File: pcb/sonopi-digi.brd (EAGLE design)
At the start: 65 x 20.3 mm, 11 parts, among them IC1 WM8804, J1 PLT133_T10W, J2 RASPI_BOARD_B+#_SMALL, X1 27MHz/15pF

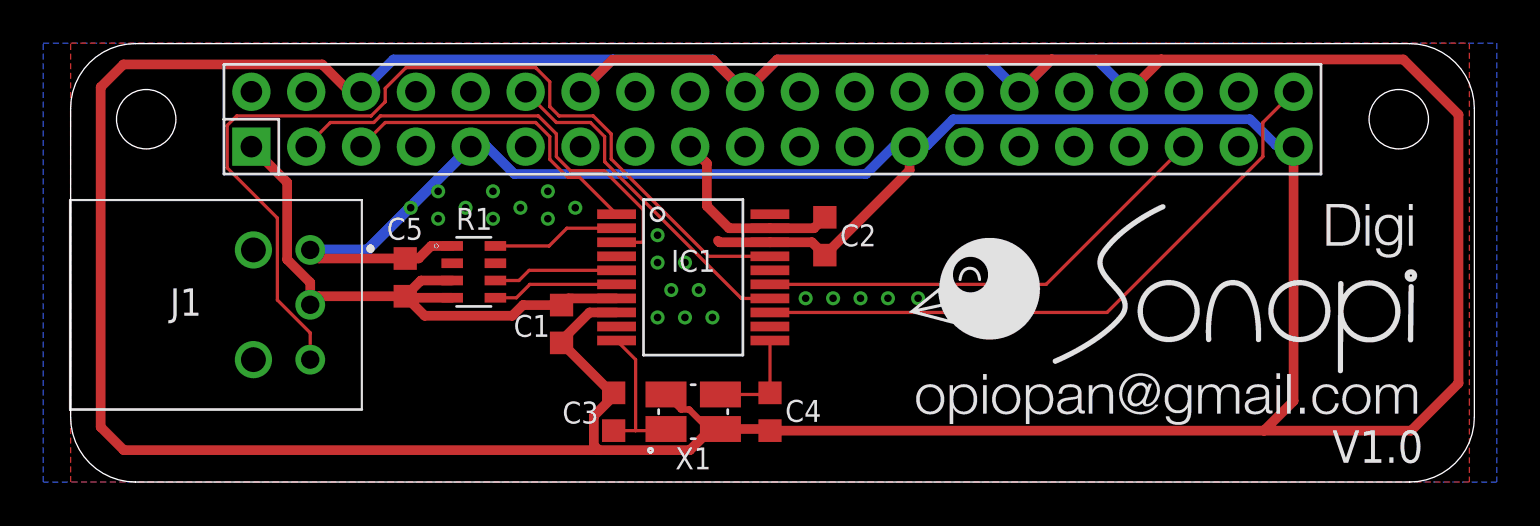
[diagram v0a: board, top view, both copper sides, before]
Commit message: fix a S/PDIF transmitter pin assign issue
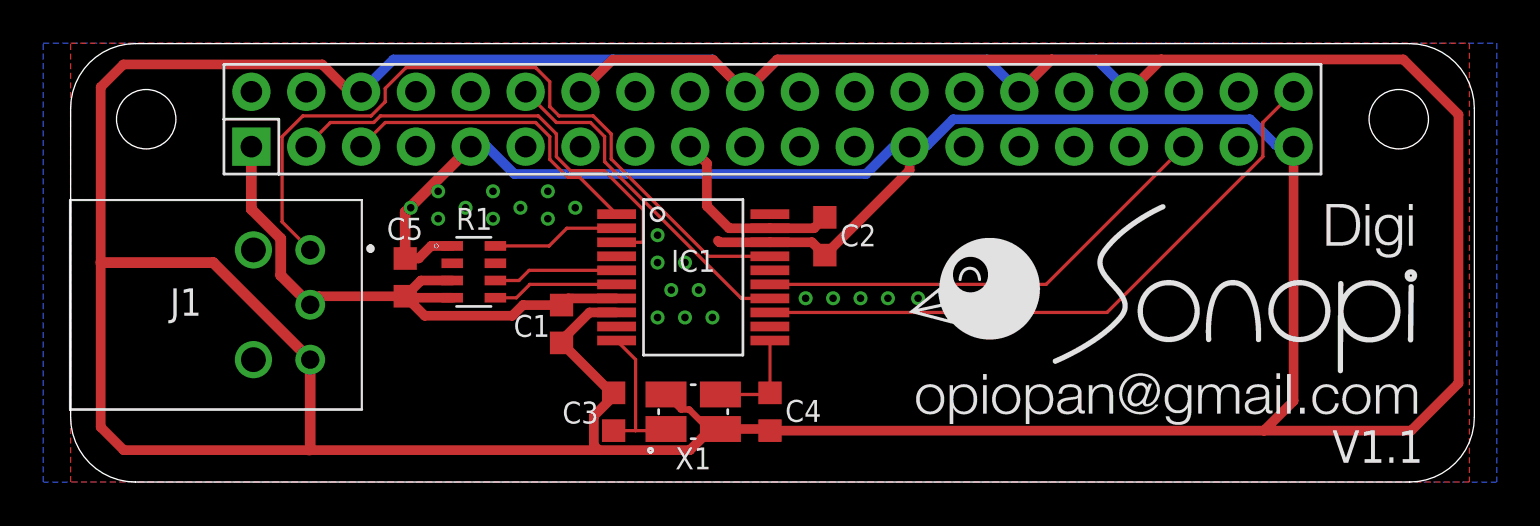
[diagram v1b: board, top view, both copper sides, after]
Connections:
- net GND: now also J1.3; no longer J1.1
- net TX0: now also J1.1; no longer J1.3
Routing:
- net TX0: track 44.0 -> 35.0 mm
- net GND: track 290.2 -> 298.4 mm
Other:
- board text added: "V1.1"
- board text removed: "V1.0"
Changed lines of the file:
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@@
 <fusionsync huburn="a.cGVyc29uYWw6dWUyYmE2M2My" projecturn="a.cGVyc29uYWw6dWUyYmE2M2MyIzIwMTgwOTE3MTQ5MTY5Mjgx" f3durn="urn:adsk.wipprod:dm.lineage:p1cDT1RiR4mqepHTu51NgA" pcbguid="6eddf113-1ed5-4f98-b271-175ee2ce72c9" lastpulledtime="" lastsyncedchangeguid="c6fdd72e-1bfb-68e5-c2ff-d97437c654df"/>
 <plain>
-<text x="58.42" y="0.889" size="1.5" layer="21">V1.0</text>
+<text x="58.42" y="0.889" size="1.5" layer="21">V1.1</text>
 </plain>
 <attributes>
@@
 <wire x1="20.4534875" y1="7.699" x2="20.9474875" y2="8.193" width="0.45" layer="1"/>
 <wire x1="16.397" y1="7.699" x2="20.4534875" y2="7.699" width="0.45" layer="1"/>
-<wire x1="11.095" y1="9.23658125" x2="11.095" y2="8.207" width="0.45" layer="1"/>
-<wire x1="10.026975" y1="10.30460625" x2="11.095" y2="9.23658125" width="0.45" layer="1"/>
-<wire x1="8.37" y1="15.53" x2="10.026975" y2="13.873025" width="0.45" layer="1"/>
-<wire x1="10.026975" y1="13.873025" x2="10.026975" y2="10.30460625" width="0.45" layer="1"/>
+<wire x1="8.37" y1="15.53" x2="8.37" y2="12.63084375" width="0.5" layer="1"/>
+<wire x1="9.7299" y1="9.5721" x2="11.095" y2="8.207" width="0.5" layer="1"/>
+<wire x1="8.37" y1="12.63084375" x2="9.7299" y2="11.27094375" width="0.5" layer="1"/>
+<wire x1="9.7299" y1="11.27094375" x2="9.7299" y2="9.5721" width="0.5" layer="1"/>
 </signal>
 <signal name="GND">
@@
 <contactref element="X1" pad="2"/>
 <contactref element="X1" pad="4"/>
-<contactref element="J1" pad="1"/>
+<contactref element="J1" pad="3"/>
 <contactref element="C5" pad="2"/>
 <contactref element="R1" pad="1"/>
 <contactref element="J2" pad="25"/>
 <contactref element="J2" pad="39"/>
-<wire x1="11.095" y1="10.747" x2="11.49" y2="10.352" width="0.45" layer="1"/>
-<wire x1="11.49" y1="10.352" x2="15.494" y2="10.352" width="0.45" layer="1"/>
 <wire x1="25.279" y1="7.852" x2="24.029" y2="7.852" width="0.45" layer="1"/>
 <wire x1="22.733" y1="6.556" x2="22.733" y2="6.443" width="0.45" layer="1"/>
@@
 <wire x1="11.6516" y1="19.3364" x2="2.4454" y2="19.3364" width="0.45" layer="1"/>
 <wire x1="12.918" y1="18.07" x2="11.6516" y2="19.3364" width="0.45" layer="1"/>
-<wire x1="1.392" y1="18.283" x2="1.392" y2="2.545" width="0.45" layer="1"/>
+<wire x1="1.392" y1="18.283" x2="1.392" y2="10.16" width="0.45" layer="1"/>
+<wire x1="1.392" y1="10.16" x2="1.392" y2="2.545" width="0.45" layer="1"/>
 <wire x1="2.4454" y1="19.3364" x2="1.392" y2="18.283" width="0.45" layer="1"/>
-<wire x1="2.4604" y1="1.4766" x2="24.449675" y2="1.4766" width="0.45" layer="1"/>
+<wire x1="2.4604" y1="1.4766" x2="11.049" y2="1.4766" width="0.45" layer="1"/>
+<wire x1="11.049" y1="1.4766" x2="24.449675" y2="1.4766" width="0.45" layer="1"/>
 <wire x1="1.392" y1="2.545" x2="2.4604" y2="1.4766" width="0.45" layer="1"/>
 <contactref element="J2" pad="34"/>
@@
 <wire x1="34.925" y1="10.507" x2="38.85" y2="14.432" width="0.45" layer="1"/>
 <wire x1="38.85" y1="14.432" x2="38.85" y2="15.53" width="0.45" layer="1"/>
-<wire x1="18.53" y1="15.53" x2="13.747" y2="10.747" width="0.5" layer="16"/>
-<wire x1="13.747" y1="10.747" x2="11.095" y2="10.747" width="0.5" layer="16"/>
 <wire x1="27.569" y1="4.054" x2="28.2666" y2="3.3564" width="0.3" layer="1"/>
 <wire x1="28.2666" y1="3.3564" x2="28.64425625" y2="3.3564" width="0.3" layer="1"/>
@@
 <wire x1="32.379" y1="11.102" x2="30.046" y2="11.102" width="0.45" layer="1"/>
 <wire x1="30.046" y1="11.102" x2="29.972" y2="11.176" width="0.45" layer="1"/>
+<wire x1="11.095" y1="5.667" x2="11.095" y2="1.5226" width="0.5" layer="1"/>
+<wire x1="11.095" y1="1.5226" x2="11.049" y2="1.4766" width="0.5" layer="1"/>
+<wire x1="11.095" y1="5.667" x2="6.602" y2="10.16" width="0.5" layer="1"/>
+<wire x1="6.602" y1="10.16" x2="1.392" y2="10.16" width="0.5" layer="1"/>
+<wire x1="18.53" y1="15.53" x2="15.494" y2="12.494" width="0.5" layer="1"/>
+<wire x1="15.494" y1="12.494" x2="15.494" y2="10.352" width="0.5" layer="1"/>
 </signal>
 <signal name="XOP">
@@
 <signal name="TX0">
 <contactref element="IC1" pad="17"/>
-<contactref element="J1" pad="3"/>
-<wire x1="21.53293125" y1="19.1876" x2="22.1876" y2="18.53293125" width="0.1524" layer="1"/>
-<wire x1="22.61865625" y1="16.9524" x2="24.1991875" y2="16.9524" width="0.1524" layer="1"/>
-<wire x1="22.1876" y1="17.38345625" x2="22.61865625" y2="16.9524" width="0.1524" layer="1"/>
-<wire x1="22.1876" y1="18.53293125" x2="22.1876" y2="17.38345625" width="0.1524" layer="1"/>
-<wire x1="29.5394" y1="10.452" x2="32.379" y2="10.452" width="0.1524" layer="1"/>
-<wire x1="25.0324" y1="16.1191875" x2="25.0324" y2="14.959" width="0.1524" layer="1"/>
-<wire x1="24.1991875" y1="16.9524" x2="25.0324" y2="16.1191875" width="0.1524" layer="1"/>
-<wire x1="25.0324" y1="14.959" x2="29.5394" y2="10.452" width="0.1524" layer="1"/>
-<wire x1="7.2524" y1="14.5463125" x2="7.2524" y2="16.5136875" width="0.1524" layer="1"/>
-<wire x1="11.095" y1="5.667" x2="11.095" y2="6.90701875" width="0.1524" layer="1"/>
-<wire x1="9.573375" y1="12.2253375" x2="7.2524" y2="14.5463125" width="0.1524" layer="1"/>
-<wire x1="11.095" y1="6.90701875" x2="9.573375" y2="8.42864375" width="0.1524" layer="1"/>
-<wire x1="9.573375" y1="8.42864375" x2="9.573375" y2="12.2253375" width="0.1524" layer="1"/>
-<wire x1="13.91293125" y1="16.9524" x2="14.5676" y2="17.60706875" width="0.1524" layer="1"/>
-<wire x1="15.52706875" y1="19.1876" x2="21.53293125" y2="19.1876" width="0.1524" layer="1"/>
-<wire x1="7.2524" y1="16.5136875" x2="7.6911125" y2="16.9524" width="0.1524" layer="1"/>
-<wire x1="7.6911125" y1="16.9524" x2="13.91293125" y2="16.9524" width="0.1524" layer="1"/>
-<wire x1="14.5676" y1="17.60706875" x2="14.5676" y2="18.22813125" width="0.1524" layer="1"/>
-<wire x1="14.5676" y1="18.22813125" x2="15.52706875" y2="19.1876" width="0.1524" layer="1"/>
+<contactref element="J1" pad="1"/>
+<wire x1="22.1876" y1="18.53293125" x2="21.53293125" y2="19.1876" width="0.1524" layer="1"/>
+<wire x1="24.1991875" y1="16.9524" x2="22.61865625" y2="16.9524" width="0.1524" layer="1"/>
+<wire x1="22.61865625" y1="16.9524" x2="22.1876" y2="17.38345625" width="0.1524" layer="1"/>
+<wire x1="22.1876" y1="17.38345625" x2="22.1876" y2="18.53293125" width="0.1524" layer="1"/>
+<wire x1="32.379" y1="10.452" x2="29.5394" y2="10.452" width="0.1524" layer="1"/>
+<wire x1="25.0324" y1="14.959" x2="25.0324" y2="16.1191875" width="0.1524" layer="1"/>
+<wire x1="25.0324" y1="16.1191875" x2="24.1991875" y2="16.9524" width="0.1524" layer="1"/>
+<wire x1="29.5394" y1="10.452" x2="25.0324" y2="14.959" width="0.1524" layer="1"/>
+<wire x1="14.5676" y1="17.60706875" x2="13.91293125" y2="16.9524" width="0.1524" layer="1"/>
+<wire x1="21.53293125" y1="19.1876" x2="15.52706875" y2="19.1876" width="0.1524" layer="1"/>
+<wire x1="14.5676" y1="18.22813125" x2="14.5676" y2="17.60706875" width="0.1524" layer="1"/>
+<wire x1="15.52706875" y1="19.1876" x2="14.5676" y2="18.22813125" width="0.1524" layer="1"/>
+<wire x1="13.91293125" y1="16.9524" x2="10.75186875" y2="16.9524" width="0.1524" layer="1"/>
+<wire x1="10.75186875" y1="16.9524" x2="9.7924" y2="15.99293125" width="0.1524" layer="1"/>
+<wire x1="9.7924" y1="12.0496" x2="11.095" y2="10.747" width="0.1524" layer="1"/>
+<wire x1="9.7924" y1="15.99293125" x2="9.7924" y2="12.0496" width="0.1524" layer="1"/>
 </signal>
 <signal name="DATA">
